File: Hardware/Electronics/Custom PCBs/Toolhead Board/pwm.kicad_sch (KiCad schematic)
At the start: 37 parts, among them U11 G20N06D52, U12 G20N06D52, U13 PCA9685BS

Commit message: Continue adding footprints
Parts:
- C50, C51, C52, C53, C54: footprint (none) -> Capacitor_SMD:C_0805_2012Metric_Pad1.18x1.45mm_HandSolder
- JP4, JP5, JP6, JP7, JP8, JP9: footprint (none) -> Jumper:SolderJumper-2_P1.3mm_Open_RoundedPad1.0x1.5mm
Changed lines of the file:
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@@
 			)
 		)
-		(property "Footprint" ""
+		(property "Footprint" "Jumper:SolderJumper-2_P1.3mm_Open_RoundedPad1.0x1.5mm"
 			(at 48.26 68.58 0)
 			(effects
@@
 			)
 		)
-		(property "Footprint" ""
+		(property "Footprint" "Capacitor_SMD:C_0805_2012Metric_Pad1.18x1.45mm_HandSolder"
 			(at 86.36 30.7848 0)
 			(effects
@@
 			)
 		)
-		(property "Footprint" ""
+		(property "Footprint" "Capacitor_SMD:C_0805_2012Metric_Pad1.18x1.45mm_HandSolder"
 			(at 67.0052 121.92 0)
 			(effects
@@
 			)
 		)
-		(property "Footprint" ""
+		(property "Footprint" "Jumper:SolderJumper-2_P1.3mm_Open_RoundedPad1.0x1.5mm"
 			(at 48.26 78.74 0)
 			(effects
@@
 			)
 		)
-		(property "Footprint" ""
+		(property "Footprint" "Capacitor_SMD:C_0805_2012Metric_Pad1.18x1.45mm_HandSolder"
 			(at 147.0152 121.92 0)
 			(effects
@@
 			)
 		)
-		(property "Footprint" ""
+		(property "Footprint" "Capacitor_SMD:C_0805_2012Metric_Pad1.18x1.45mm_HandSolder"
 			(at 106.3752 121.92 0)
 			(effects
@@
 			)
 		)
-		(property "Footprint" ""
+		(property "Footprint" "Capacitor_SMD:C_0805_2012Metric_Pad1.18x1.45mm_HandSolder"
 			(at 26.3652 121.92 0)
 			(effects
@@
 			)
 		)
-		(property "Footprint" ""
+		(property "Footprint" "Jumper:SolderJumper-2_P1.3mm_Open_RoundedPad1.0x1.5mm"
 			(at 48.26 83.82 0)
 			(effects
@@
 			)
 		)
-		(property "Footprint" ""
+		(property "Footprint" "Jumper:SolderJumper-2_P1.3mm_Open_RoundedPad1.0x1.5mm"
 			(at 48.26 63.5 0)
 			(effects
@@
 			)
 		)
-		(property "Footprint" ""
+		(property "Footprint" "Jumper:SolderJumper-2_P1.3mm_Open_RoundedPad1.0x1.5mm"
 			(at 48.26 58.42 0)
 			(effects
@@
 			)
 		)
-		(property "Footprint" ""
+		(property "Footprint" "Jumper:SolderJumper-2_P1.3mm_Open_RoundedPad1.0x1.5mm"
 			(at 48.26 73.66 0)
 			(effects

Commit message: Get basic Toolhead Board outline
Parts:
- U11, U12: footprint (none) -> lib:WDFN-8-1EP_6x5mm_P1.27mm_EP3.4x4mm_No_Center_Pad
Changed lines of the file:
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@@
 			)
 		)
-		(property "Footprint" ""
+		(property "Footprint" "lib:WDFN-8-1EP_6x5mm_P1.27mm_EP3.4x4mm_No_Center_Pad"
 			(at 168.91 40.64 0)
 			(effects
@@
 			)
 		)
-		(property "Footprint" ""
+		(property "Footprint" "lib:WDFN-8-1EP_6x5mm_P1.27mm_EP3.4x4mm_No_Center_Pad"
 			(at 168.91 54.61 0)
 			(effects

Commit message: Update toolhead board layout
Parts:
- U11, U12: footprint lib:WDFN-8-1EP_6x5mm_P1.27mm_EP3.4x4mm_No_Center_Pad -> Library:WDFN-8-1EP_6x5mm_P1.27mm_EP3.4x4mm_No_Center_Pad
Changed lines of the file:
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@@
 			)
 		)
-		(property "Footprint" "lib:WDFN-8-1EP_6x5mm_P1.27mm_EP3.4x4mm_No_Center_Pad"
+		(property "Footprint" "Library:WDFN-8-1EP_6x5mm_P1.27mm_EP3.4x4mm_No_Center_Pad"
 			(at 168.91 40.64 0)
 			(effects
@@
 			)
 		)
-		(property "Footprint" "lib:WDFN-8-1EP_6x5mm_P1.27mm_EP3.4x4mm_No_Center_Pad"
+		(property "Footprint" "Library:WDFN-8-1EP_6x5mm_P1.27mm_EP3.4x4mm_No_Center_Pad"
 			(at 168.91 54.61 0)
 			(effects

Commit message: Update toolhead board yet again
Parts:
- removed JP4, JP5, JP6, JP7, JP8, JP9: SolderJumper_2_Open, Jumper:SolderJumper-2_P1.3mm_Open_RoundedPad1.0x1.5mm, symbol Jumper:SolderJumper_2_Open
- removed R46, R48, R53, R54, R55, R56: 10k, Resistor_SMD:R_0603_1608Metric_Pad0.98x0.95mm_HandSolder, symbol Device:R
- renumbered R47 to R46, R49 to R47, R50 to R48, R51 to R49, R52 to R50, R57 to R51, R58 to R52, R59 to R53, R60 to R54
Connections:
- no-connect marks 4 -> 10

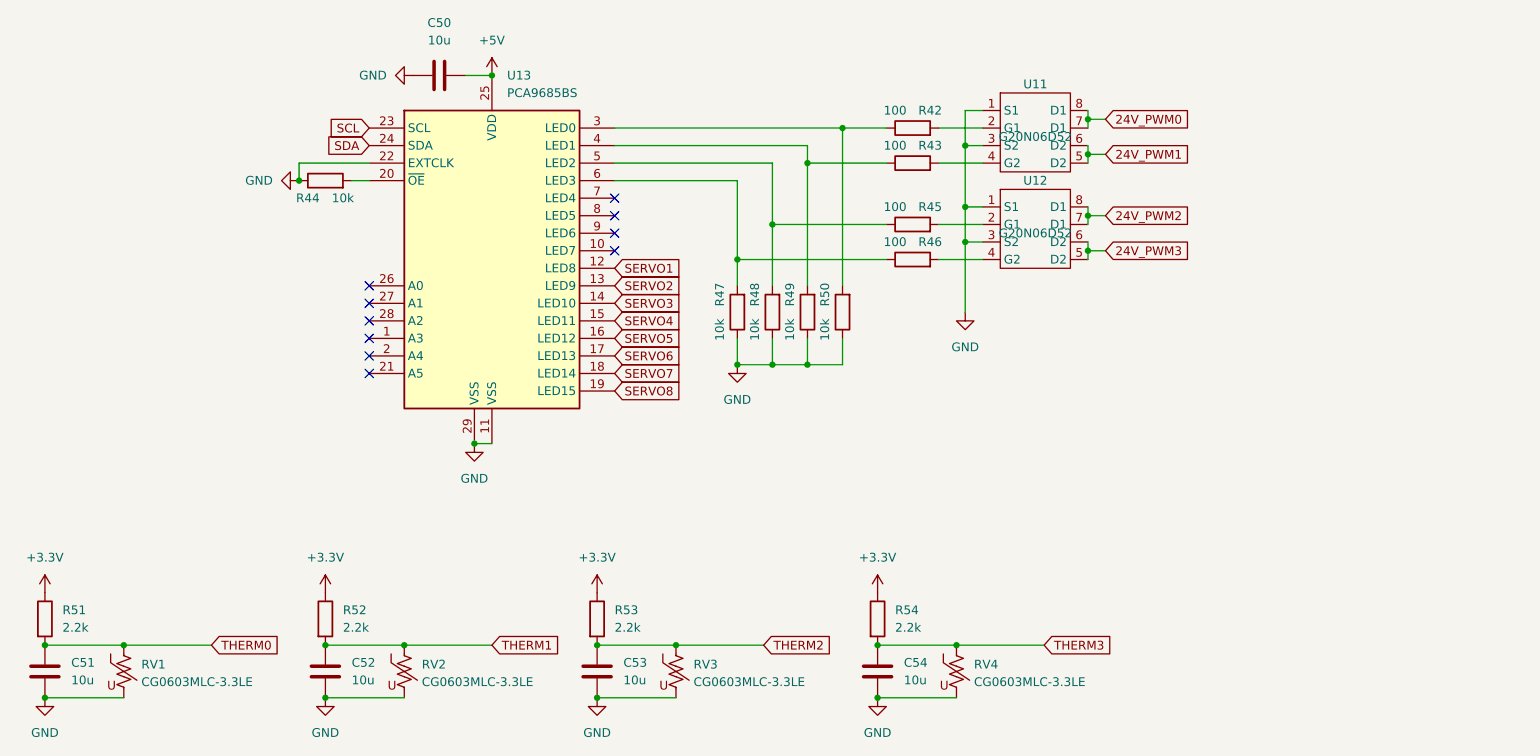
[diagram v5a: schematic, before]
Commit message: Begin replacing CAN transceiver
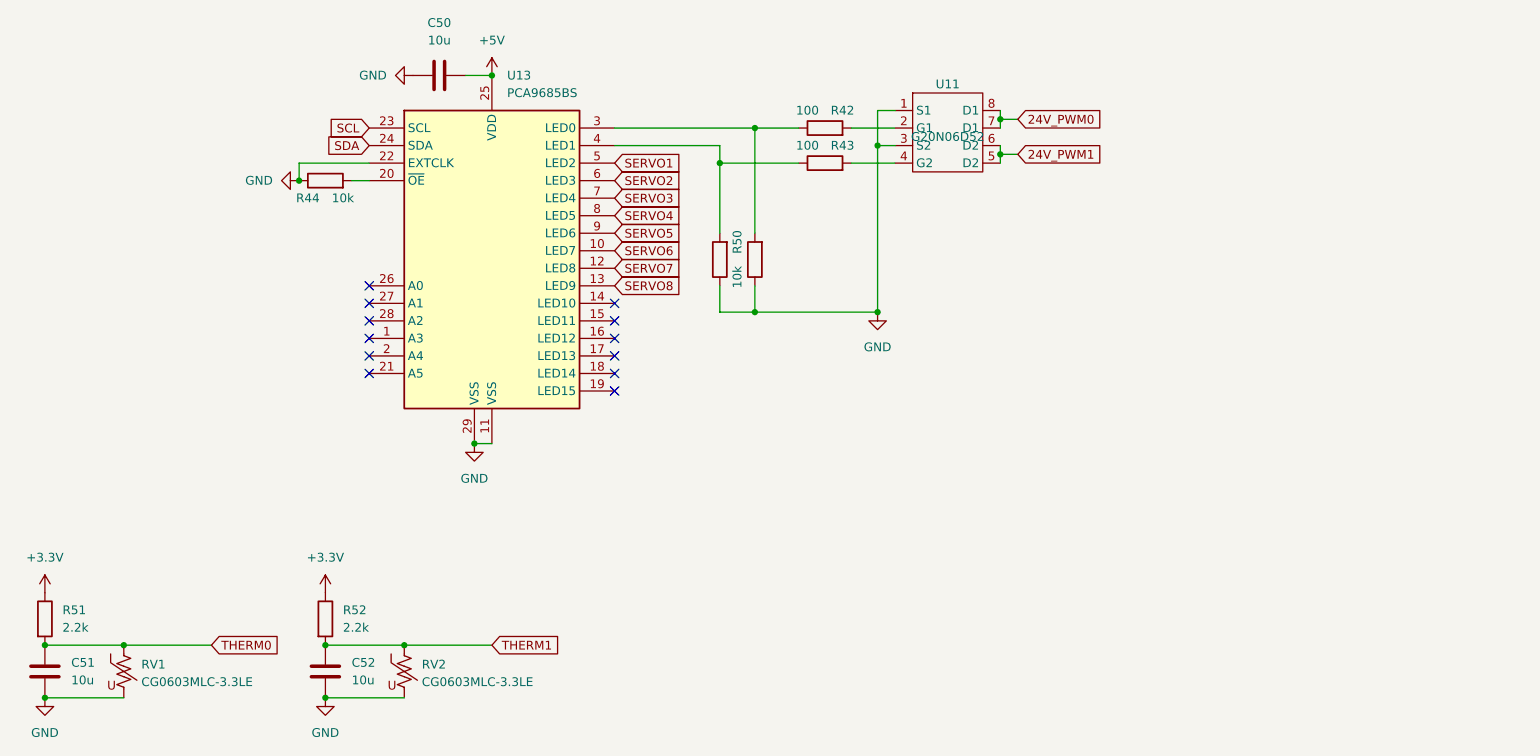
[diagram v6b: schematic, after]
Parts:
- removed C53, C54: 10u, Capacitor_SMD:C_0805_2012Metric_Pad1.18x1.45mm_HandSolder, symbol Device:C
- removed R45, R46: 100, Resistor_SMD:R_0603_1608Metric_Pad0.98x0.95mm_HandSolder, symbol Device:R
- removed R47, R48: 10k, Resistor_SMD:R_0603_1608Metric_Pad0.98x0.95mm_HandSolder, symbol Device:R
- removed R53, R54: 2.2k, Resistor_SMD:R_0603_1608Metric_Pad0.98x0.95mm_HandSolder, symbol Device:R
- removed RV3, RV4: CG0603MLC-3.3LE, Resistor_SMD:R_0603_1608Metric_Pad0.98x0.95mm_HandSolder, symbol Device:Varistor_US
- removed U12: G20N06D52, Library:WDFN-8-1EP_6x5mm_P1.27mm_EP3.4x4mm_No_Center_Pad, symbol symbols:G20N06D52
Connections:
- net SERVO1: now also U13.5 (LED2); no longer U13.12 (LED8)
- net SERVO2: now also U13.6 (LED3); no longer U13.13 (LED9)
- net SERVO3: now also U13.7 (LED4); no longer U13.14 (LED10)
- net SERVO4: now also U13.8 (LED5); no longer U13.15 (LED11)
- net SERVO5: now also U13.9 (LED6); no longer U13.16 (LED12)
- net SERVO6: now also U13.10 (LED7); no longer U13.17 (LED13)
- net SERVO7: now also U13.12 (LED8); no longer U13.18 (LED14)
- net SERVO8: now also U13.13 (LED9); no longer U13.19 (LED15)
- no-connect marks 10 -> 12
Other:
- moved on the sheet: R42, R43, R50, U11

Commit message: Update toolhead schematic+layout and add tolerances to base
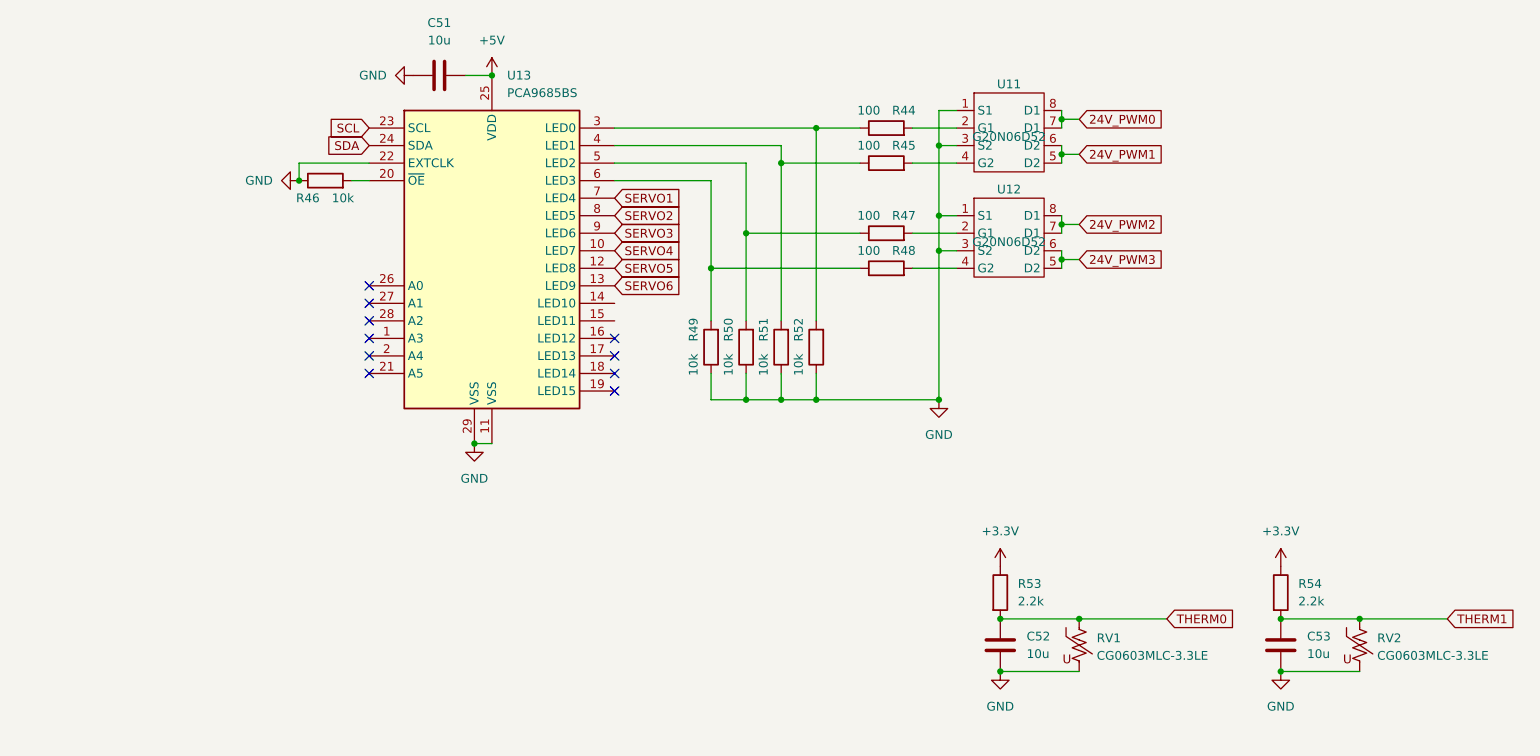
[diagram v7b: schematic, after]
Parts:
- added R47, R48: 100, Resistor_SMD:R_0603_1608Metric_Pad0.98x0.95mm_HandSolder, symbol Device:R
- added R50, R51: 10k, Resistor_SMD:R_0603_1608Metric_Pad0.98x0.95mm_HandSolder, symbol Device:R
- added U12: G20N06D52, Library:WDFN-8-1EP_6x5mm_P1.27mm_EP3.4x4mm_No_Center_Pad, symbol symbols:G20N06D52
- renumbered C50 to C51, C51 to C52, C52 to C53, R42 to R44, R43 to R45, R44 to R46, R50 to R52, R51 to R53, R52 to R54
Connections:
- net SERVO7 is gone; now on net SERVO5: U13.12 (LED8)
- net SERVO8 is gone; now on net SERVO6: U13.13 (LED9)
- net GND: now also R50.1, R51.1, U12.1 (S1), U12.3 (S2)
- net SERVO1: now also U13.7 (LED4); no longer U13.5 (LED2)
- net SERVO2: now also U13.8 (LED5); no longer U13.6 (LED3)
- net SERVO3: now also U13.9 (LED6); no longer U13.7 (LED4)
- net SERVO4: now also U13.10 (LED7); no longer U13.8 (LED5)
- net SERVO5: no longer U13.9 (LED6)
- net SERVO6: no longer U13.10 (LED7)
- net at R45.1, U13.4 (LED1): now also R51.2; no longer R49.2
- new net: R47.2, U12.2 (G1)
- new net: R48.2, U12.4 (G2)
- new net: R47.1, R50.2, U13.5 (LED2)
- new net: R48.1, R49.2, U13.6 (LED3)
- new net 24V_PWM2: U12.7 (D1), U12.8 (D1)
- new net 24V_PWM3: U12.5 (D2), U12.6 (D2)
- no-connect marks 12 -> 10
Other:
- moved on the sheet: C52, C53, R44, R45, R52, R53, R54, RV1, RV2, U11

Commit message: Update layout a bit more
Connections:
- no-connect marks 10 -> 12
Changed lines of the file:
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@@
+	)
+	(no_connect
+		(at 107.95 67.31)
 	)
 	(no_connect
@@
 	)
 	(no_connect
+		(at 107.95 64.77)
+	)
+	(no_connect
